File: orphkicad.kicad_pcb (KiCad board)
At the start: 2 copper layers, 21 x 51 mm, 43 parts, among them J1 USB_C_Receptacle_USB2.0_16P, SW1 BTN_BOOT, SW2 BTN_RST, SW3 BTN_USR, U1 RP2040, U2 W25Q16JVUXIQ, U3 USBLC6-2SC6, U4 ME2135A33M6G, X1 X322512MSB4SI

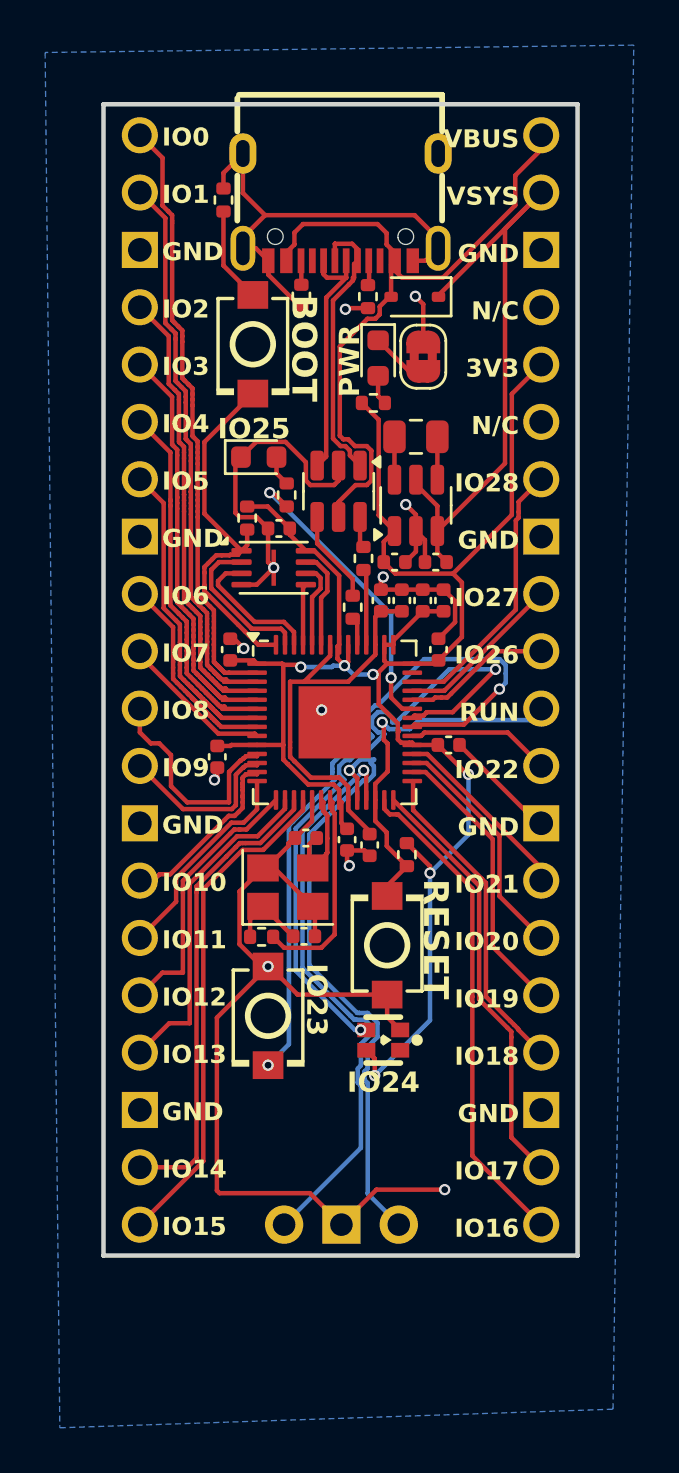
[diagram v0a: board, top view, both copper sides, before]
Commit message: Dejankifies back plane routing
Routing on the back plane is now a little less janky, at the cost of a more segmented back plane.
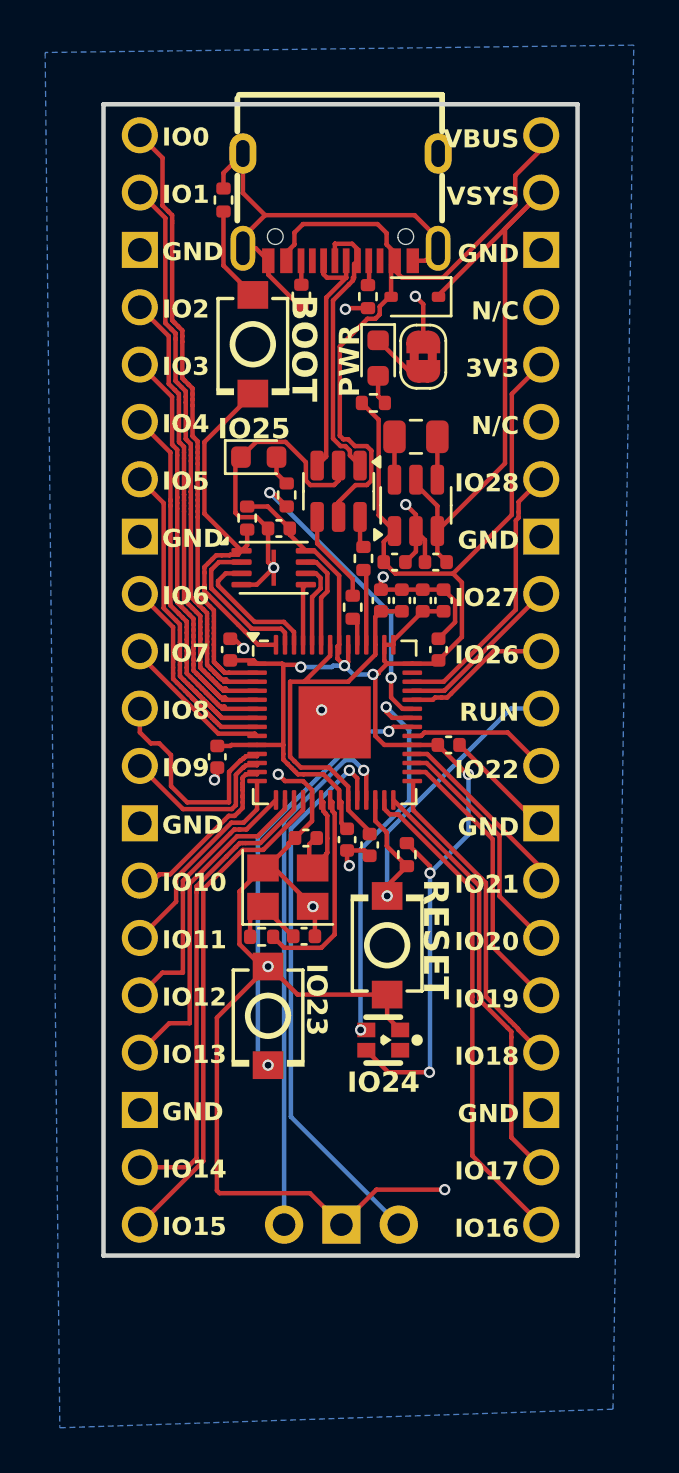
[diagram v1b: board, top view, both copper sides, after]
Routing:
- net GPIO24: track 29.1 -> 17.1 mm
- net GPIO23: track 31.1 -> 19.1 mm
- net SWCLK: track 27.2 -> 24.6 mm
- net GND: track 101.7 -> 104.0 mm, vias 11 -> 13
- net SWD: track 25.8 -> 24.1 mm
- net 3V3: track 88.4 -> 89.7 mm
- net RUN: track 16.5 -> 17.1 mm
